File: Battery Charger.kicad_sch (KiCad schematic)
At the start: 40 parts

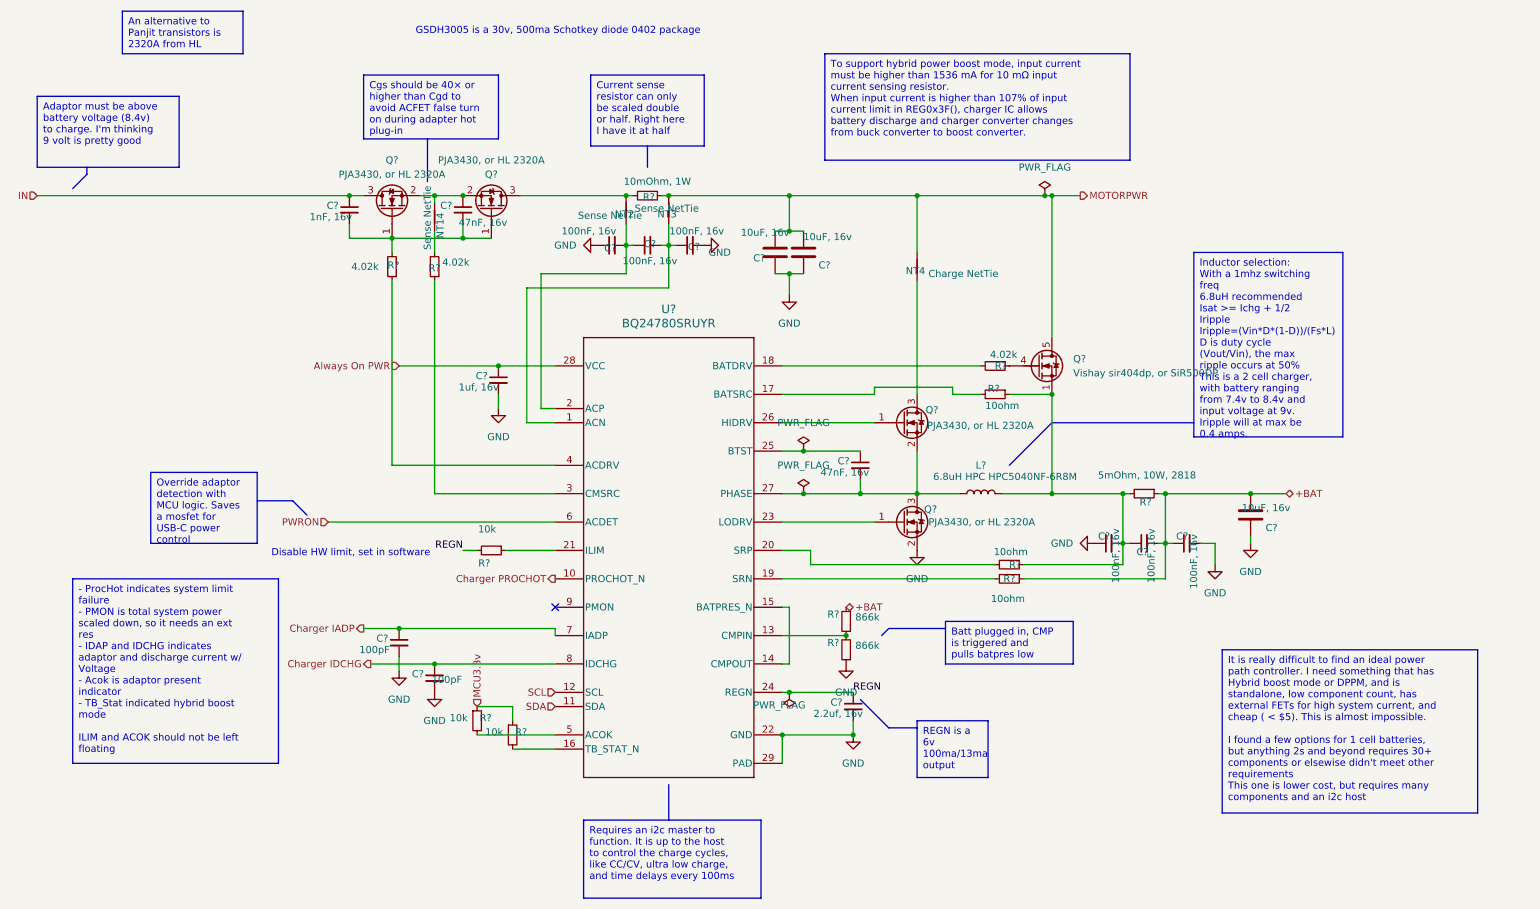
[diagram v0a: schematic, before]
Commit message: Updated to kicad 9
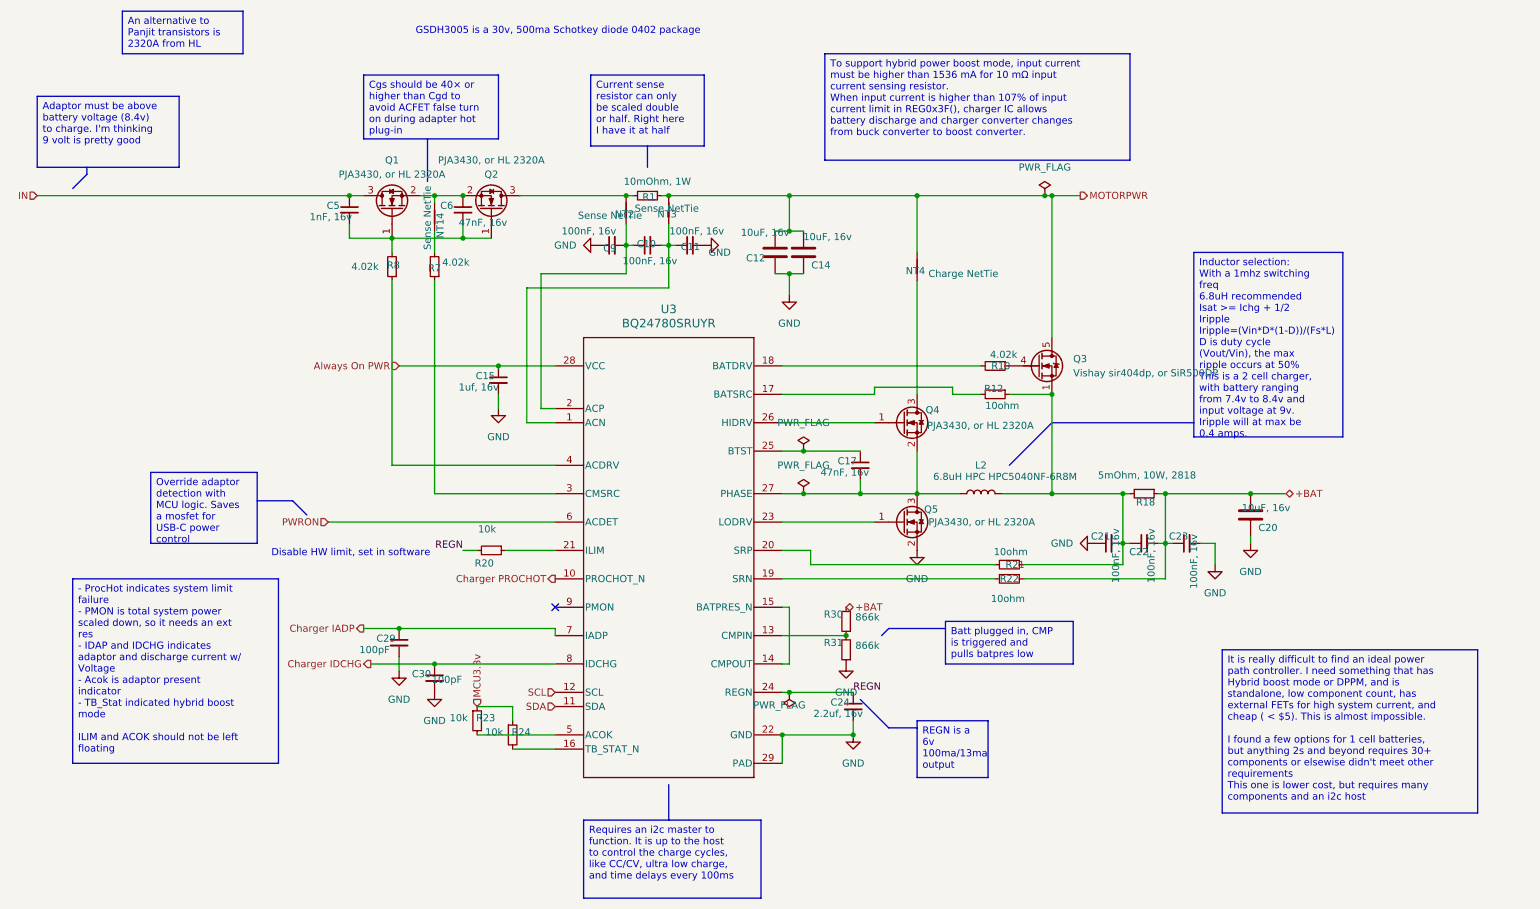
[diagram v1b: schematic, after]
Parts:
- Q1, Q2, Q4, Q5: renamed from Q?; symbol Device:Q_NMOS_GSD -> Transistor_FET:Q_NMOS_GSD
- gave numbers to parts that had none: 32

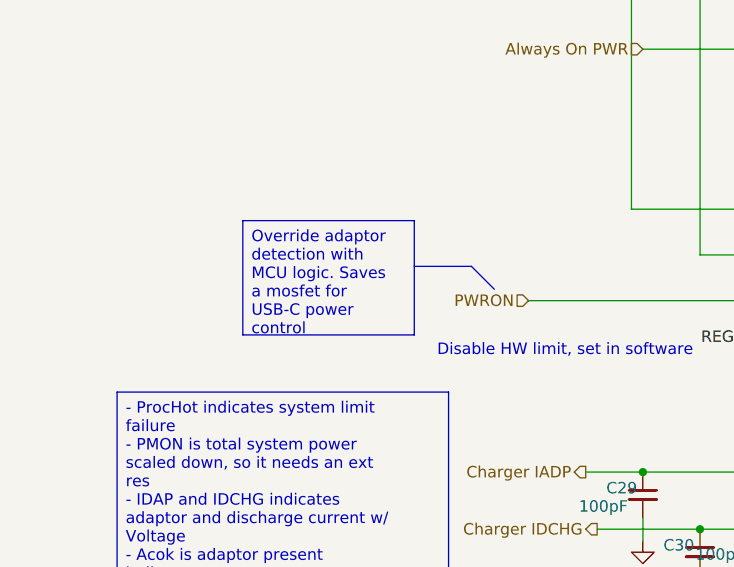
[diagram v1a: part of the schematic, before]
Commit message: Added MCU boot button, 3v3 power enable, and pulldown on adaptor enable
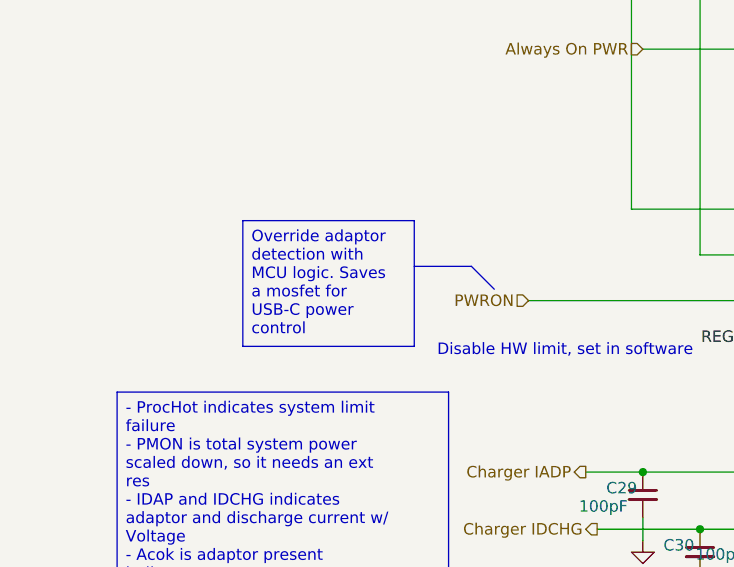
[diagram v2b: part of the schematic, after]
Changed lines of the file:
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@@
 		(exclude_from_sim no)
 		(at 39.37 104.14 0)
-		(size 19.05 12.7)
+		(size 19.05 13.97)
 		(margins 0.9525 0.9525 0.9525 0.9525)
 		(stroke

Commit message: Revert update of pmosfets with large pad 5
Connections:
- net MOTORPWR: no longer Q3.6 (D), Q3.7 (D), Q3.8 (D)
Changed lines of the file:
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@@
 		(pin "4"
-		)
-		(pin "7"
-		)
-		(pin "8"
 		)
 		(pin "5"
 		)
-		(pin "6"
-		)
 		(instances
